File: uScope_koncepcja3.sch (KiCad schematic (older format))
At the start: 47 parts

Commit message: - schematic as hierarchical - added cache lib
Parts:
- renumbered V_Focus to V_Focus?, V_K to V_K?, V_Wh to V_Wh?
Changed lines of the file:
@@
 EESchema Schematic File Version 4
+LIBS:uScope-cache
 EELAYER 26 0
 EELAYER END
 $Descr A4 11693 8268
 encoding utf-8
-Sheet 1 1
+Sheet 1 5
 Title ""
 Date "2020-08-14"
@@
 $EndComp
 $Comp
-L pspice:VSOURCE V_K
+L pspice:VSOURCE V_K?
 U 1 1 5F36B478
 P 2100 2500
-F 0 "V_K" H 1734 2454 50  0000 R CNN
+F 0 "V_K?" H 1734 2454 50  0000 R CNN
 F 1 "4.5 kV" H 1734 2545 50  0000 R CNN
 F 2 "" H 2100 2500 50  0001 C CNN
@@
 $EndComp
 $Comp
-L pspice:VSOURCE V_Wh
+L pspice:VSOURCE V_Wh?
 U 1 1 5F36B607
 P 3050 2500
-F 0 "V_Wh" H 2684 2454 50  0000 R CNN
+F 0 "V_Wh?" H 2684 2454 50  0000 R CNN
 F 1 "5 kV" H 2684 2545 50  0000 R CNN
 F 2 "" H 3050 2500 50  0001 C CNN
@@
 $EndComp
 $Comp
-L pspice:VSOURCE V_Focus
+L pspice:VSOURCE V_Focus?
 U 1 1 5F36B645
 P 4200 2500
-F 0 "V_Focus" H 4428 2546 50  0000 L CNN
+F 0 "V_Focus?" H 4428 2546 50  0000 L CNN
 F 1 "500 V" H 4428 2455 50  0000 L CNN
 F 2 "" H 4200 2500 50  0001 C CNN

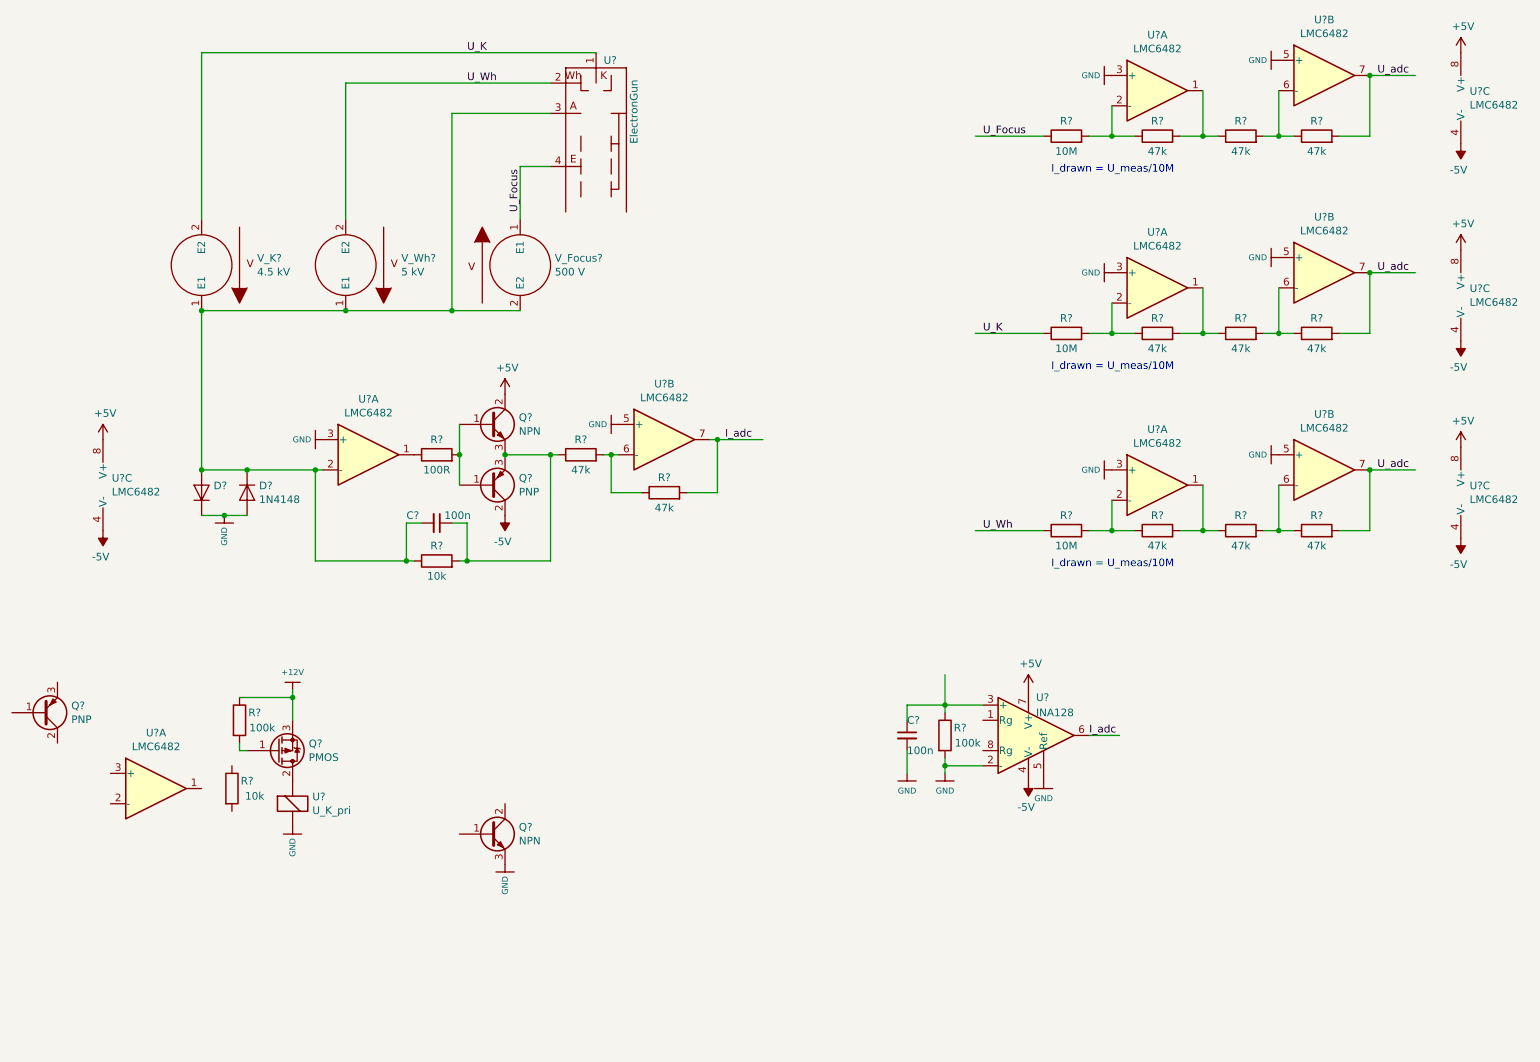
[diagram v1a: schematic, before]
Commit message: - moved voltmeters to separate sheet - hierarchical sheets
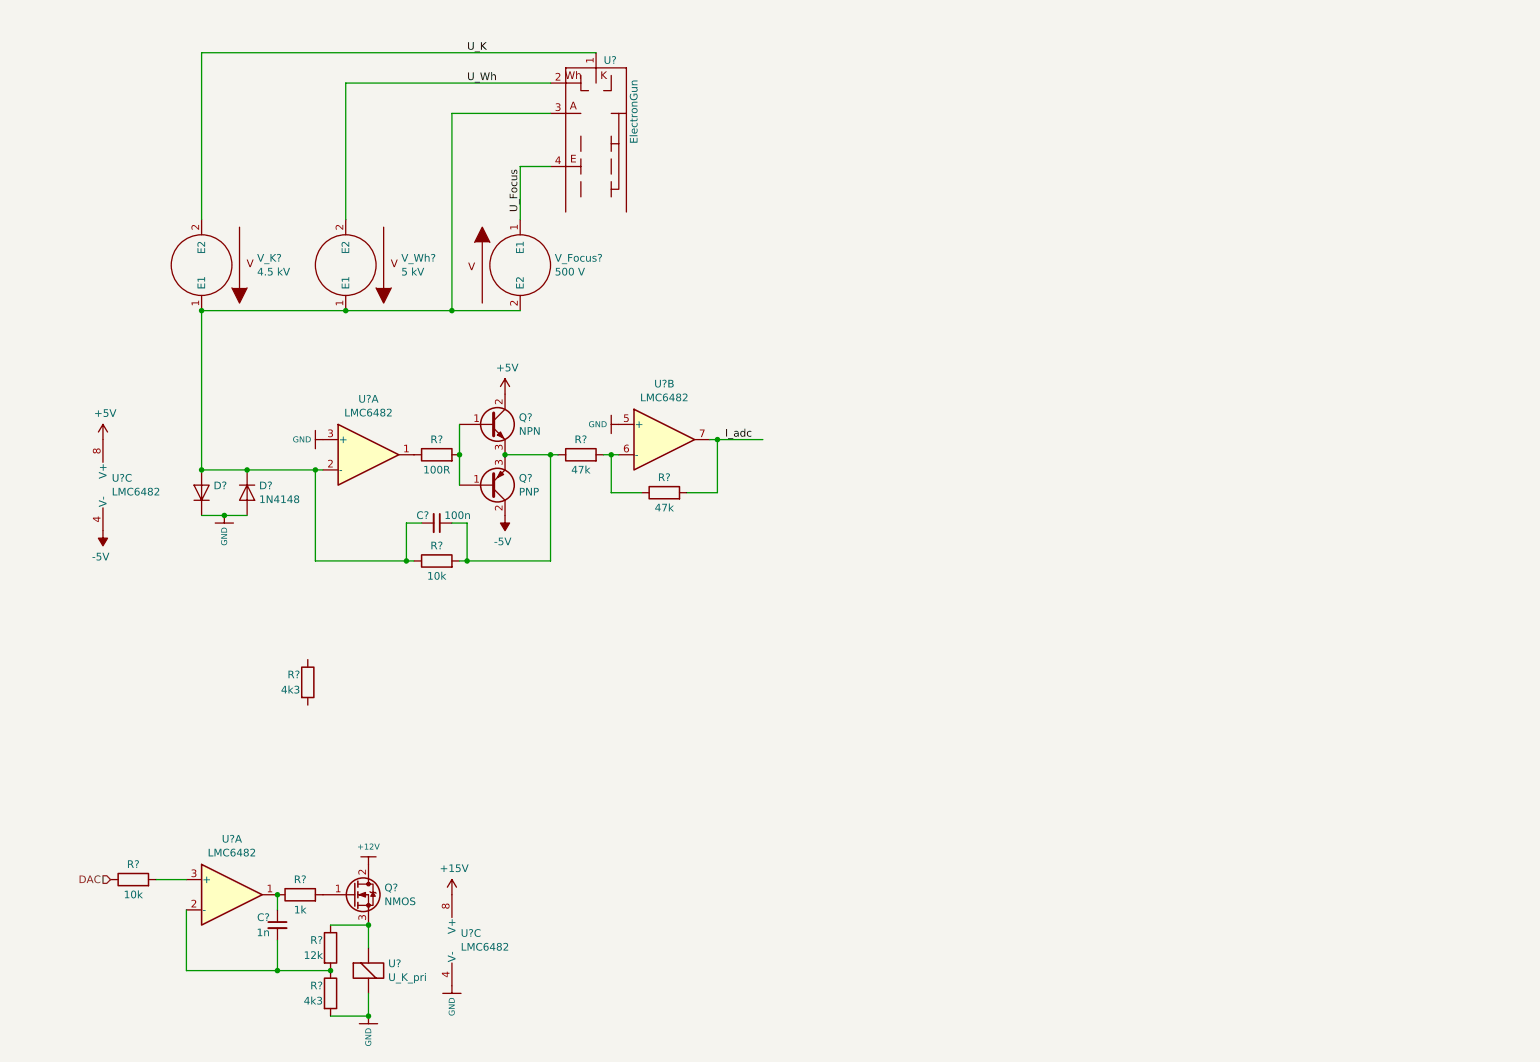
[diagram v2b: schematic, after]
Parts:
- removed C?: 100n, symbol Device:C_Small
- removed Q?: NPN, symbol Device:Q_NPN_BCE
- removed Q?: PNP, symbol Device:Q_PNP_BCE
- removed Q?: PMOS, symbol Device:Q_PMOS_GDS
- removed R? (x9): 47k, symbol Device:R
- removed R? (x3): 10M, symbol Device:R
- removed R? (x2): 100k, symbol Device:R
- removed R?: 10k, symbol Device:R
- removed U? (x9): LMC6482, symbol Amplifier_Operational:LMC6482
- removed U?: INA128, symbol Amplifier_Instrumentation:INA128
- added C?: 1n, symbol Device:C_Small
- added Q?: NMOS, symbol Device:Q_NMOS_GDS
- added R?: 10k, symbol Device:R
- added R?: 1k, symbol Device:R
- added R?: 12k, symbol Device:R
- added R? (x2): 4k3, symbol Device:R
- added U?: LMC6482, symbol Amplifier_Operational:LMC6482
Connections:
- net labels added: +15V, DAC
- net labels removed: U_adc
- wire segments 93 -> 49
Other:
- note removed: "I_drawn = U_meas/10M"
- moved on the sheet: U?, U?A

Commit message: - added DC/DC converter to library, - moved ammeter & drivers to sub-sheet, - further develop
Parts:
- removed C?: 100n, symbol Device:C_Small
- removed C?: 1n, symbol Device:C_Small
- removed D? (x2): 1N4148, Diode_THT:D_DO-35_SOD27_P7.62mm_Horizontal, symbol Diode:1N4148
- removed Q?: NPN, symbol Device:Q_NPN_BCE
- removed Q?: PNP, symbol Device:Q_PNP_BCE
- removed Q?: NMOS, symbol Device:Q_NMOS_GDS
- removed R? (x2): 10k, symbol Device:R
- removed R?: 100R, symbol Device:R
- removed R?: 1k, symbol Device:R
- removed R?: 12k, symbol Device:R
- removed R? (x2): 47k, symbol Device:R
- removed R? (x2): 4k3, symbol Device:R
- removed U?: ElectronGun, symbol uScope:ElectronGun
- removed U? (x5): LMC6482, symbol Amplifier_Operational:LMC6482
- removed U?: U_K_pri, symbol Device:Electromagnetic_Actor
- removed V_Focus?: 500 V, symbol pspice:VSOURCE
- removed V_K?: 4.5 kV, symbol pspice:VSOURCE
- removed V_Wh?: 5 kV, symbol pspice:VSOURCE
